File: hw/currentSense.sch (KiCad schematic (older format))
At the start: 2 parts, among them U601 ZXCT1086

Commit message: first pcb revision ready to order
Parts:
- renumbered U601 to U501
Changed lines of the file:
@@
 LIBS:usevolt
 LIBS:wurth_elektronik_LED
+LIBS:csb-cache
 EELAYER 26 0
 EELAYER END
@@
 $EndDescr
 $Comp
-L ZXCT1086 U601
+L ZXCT1086 U501
 U 1 1 594D8B7D
 P 5450 3600
-AR Path="/58BE52C9/58BE8E4D/594D8B7D" Ref="U601"  Part="1"
-AR Path="/58BE52C9/58BE8E7A/594D8B7D" Ref="U701"  Part="1"
-AR Path="/58BE52C9/5955DE03/594D8B7D" Ref="U801"  Part="1"
-AR Path="/58C7B0A8/594D8B80/594D8B7D" Ref="U1001"  Part="1"
-AR Path="/58C7B0A8/594D8B83/594D8B7D" Ref="U1101"  Part="1"
-AR Path="/58C7B0A8/58BE8E88/594D8B7D" Ref="U1201"  Part="1"
+AR Path="/59542AAB/595CED4D/594D8B7D" Ref="U501"  Part="1"
+AR Path="/59542AAB/58BE8E7A/594D8B7D" Ref="U601"  Part="1"
+AR Path="/59542AAB/58BE8E88/594D8B7D" Ref="U701"  Part="1"
+AR Path="/59542AAB/58BE8E96/594D8B7D" Ref="U801"  Part="1"
+AR Path="/5954FB0E/58BE8E4D/594D8B7D" Ref="U1001"  Part="1"
+AR Path="/5954FB0E/595CED50/594D8B7D" Ref="U1101"  Part="1"
+AR Path="/5954FB0E/595CED51/594D8B7D" Ref="U1201"  Part="1"
 F 0 "U1201" H 5425 3887 60  0000 C CNN
 F 1 "ZXCT1086" H 5425 3781 60  0000 C CNN
@@
 $EndComp
 $Comp
-L GND #PWR602
+L GND #PWR024
 U 1 1 594D8B7E
 P 5050 4000
-AR Path="/58BE52C9/58BE8E4D/594D8B7E" Ref="#PWR602"  Part="1"
-AR Path="/58BE52C9/58BE8E7A/594D8B7E" Ref="#PWR702"  Part="1"
-AR Path="/58BE52C9/5955DE03/594D8B7E" Ref="#PWR802"  Part="1"
-AR Path="/58C7B0A8/594D8B80/594D8B7E" Ref="#PWR1002"  Part="1"
-AR Path="/58C7B0A8/594D8B83/594D8B7E" Ref="#PWR1102"  Part="1"
-AR Path="/58C7B0A8/58BE8E88/594D8B7E" Ref="#PWR1202"  Part="1"
-F 0 "#PWR1202" H 5050 3750 50  0001 C CNN
+AR Path="/59542AAB/595CED4D/594D8B7E" Ref="#PWR024"  Part="1"
+AR Path="/59542AAB/58BE8E7A/594D8B7E" Ref="#PWR026"  Part="1"
+AR Path="/59542AAB/58BE8E88/594D8B7E" Ref="#PWR028"  Part="1"
+AR Path="/59542AAB/58BE8E96/594D8B7E" Ref="#PWR030"  Part="1"
+AR Path="/5954FB0E/58BE8E4D/594D8B7E" Ref="#PWR035"  Part="1"
+AR Path="/5954FB0E/595CED50/594D8B7E" Ref="#PWR037"  Part="1"
+AR Path="/5954FB0E/595CED51/594D8B7E" Ref="#PWR039"  Part="1"
+F 0 "#PWR039" H 5050 3750 50  0001 C CNN
 F 1 "GND" H 5055 3827 50  0000 C CNN
 F 2 "" H 5050 4000 50  0000 C CNN
@@
 $EndComp
 $Comp
-L +3V3 #PWR601
+L +3V3 #PWR025
 U 1 1 589841AE
 P 5050 3350
-AR Path="/58BE52C9/58BE8E4D/589841AE" Ref="#PWR601"  Part="1"
-AR Path="/58BE52C9/58BE8E7A/589841AE" Ref="#PWR701"  Part="1"
-AR Path="/58BE52C9/5955DE03/589841AE" Ref="#PWR801"  Part="1"
-AR Path="/58C7B0A8/594D8B80/589841AE" Ref="#PWR1001"  Part="1"
-AR Path="/58C7B0A8/594D8B83/589841AE" Ref="#PWR1101"  Part="1"
-AR Path="/58C7B0A8/58BE8E88/589841AE" Ref="#PWR1201"  Part="1"
-F 0 "#PWR1201" H 5050 3200 50  0001 C CNN
+AR Path="/59542AAB/595CED4D/589841AE" Ref="#PWR025"  Part="1"
+AR Path="/59542AAB/58BE8E7A/589841AE" Ref="#PWR027"  Part="1"
+AR Path="/59542AAB/58BE8E88/589841AE" Ref="#PWR029"  Part="1"
+AR Path="/59542AAB/58BE8E96/589841AE" Ref="#PWR031"  Part="1"
+AR Path="/5954FB0E/58BE8E4D/589841AE" Ref="#PWR036"  Part="1"
+AR Path="/5954FB0E/595CED50/589841AE" Ref="#PWR038"  Part="1"
+AR Path="/5954FB0E/595CED51/589841AE" Ref="#PWR040"  Part="1"
+F 0 "#PWR040" H 5050 3200 50  0001 C CNN
 F 1 "+3V3" H 5065 3523 50  0000 C CNN
 F 2 "" H 5050 3350 50  0000 C CNN
@@
 AR Path="/589A417E/589858BC" Ref="R?"  Part="1"
 AR Path="/58BE52C9/58BE8E88/589858BC" Ref="R?"  Part="1"
-AR Path="/58BE52C9/58BE8E4D/589858BC" Ref="R601"  Part="1"
-AR Path="/58BE52C9/58BE8E7A/589858BC" Ref="R701"  Part="1"
+AR Path="/58BE52C9/58BE8E4D/589858BC" Ref="R?"  Part="1"
+AR Path="/58BE52C9/58BE8E7A/589858BC" Ref="R?"  Part="1"
 AR Path="/58BE52C9/58BE8E96/589858BC" Ref="R?"  Part="1"
 AR Path="/58C7B0A8/58BE8E4D/589858BC" Ref="R?"  Part="1"
 AR Path="/58C7B0A8/58BE8E7A/589858BC" Ref="R?"  Part="1"
-AR Path="/58C7B0A8/58BE8E88/589858BC" Ref="R1201"  Part="1"
+AR Path="/58C7B0A8/58BE8E88/589858BC" Ref="R?"  Part="1"
 AR Path="/58C7B0A8/58BE8E96/589858BC" Ref="R?"  Part="1"
-AR Path="/58BE52C9/5955DE03/589858BC" Ref="R801"  Part="1"
-AR Path="/58C7B0A8/594D8B80/589858BC" Ref="R1001"  Part="1"
-AR Path="/58C7B0A8/594D8B83/589858BC" Ref="R1101"  Part="1"
+AR Path="/58BE52C9/5955DE03/589858BC" Ref="R?"  Part="1"
+AR Path="/58C7B0A8/594D8B80/589858BC" Ref="R?"  Part="1"
+AR Path="/58C7B0A8/594D8B83/589858BC" Ref="R?"  Part="1"
+AR Path="/59542AAB/58BE8E4D/589858BC" Ref="R?"  Part="1"
+AR Path="/59542AAB/58BE8E7A/589858BC" Ref="R601"  Part="1"
+AR Path="/59542AAB/58BE8E88/589858BC" Ref="R701"  Part="1"
+AR Path="/59542AAB/58BE8E96/589858BC" Ref="R801"  Part="1"
+AR Path="/5954FB0E/58BE8E4D/589858BC" Ref="R1001"  Part="1"
+AR Path="/5954FB0E/58BE8E7A/589858BC" Ref="R?"  Part="1"
+AR Path="/5954FB0E/58BE8E88/589858BC" Ref="R?"  Part="1"
+AR Path="/59542AAB/595CED4D/589858BC" Ref="R501"  Part="1"
+AR Path="/5954FB0E/595CED50/589858BC" Ref="R1101"  Part="1"
+AR Path="/5954FB0E/595CED51/589858BC" Ref="R1201"  Part="1"
 F 0 "R1201" V 6208 3508 45  0000 L CNN
 F 1 "LRMAT2512-R002FT4" V 6292 3508 45  0000 L CNN

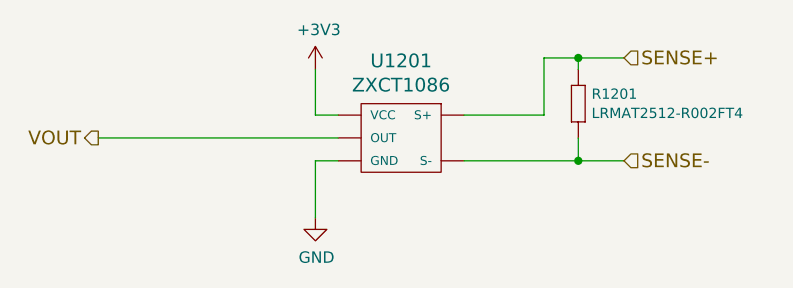
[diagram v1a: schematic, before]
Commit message: sw directory created, oil cooler added in hw
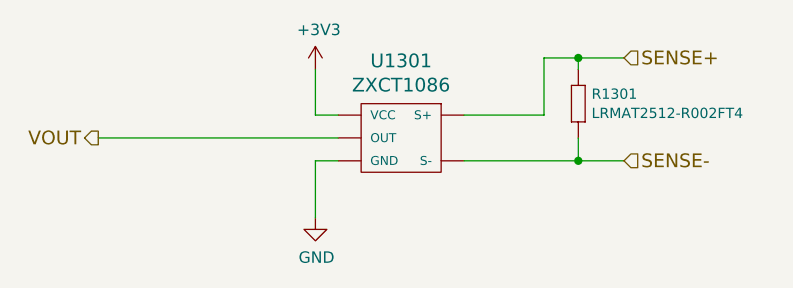
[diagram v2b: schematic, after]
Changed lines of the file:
@@
 $Descr A4 11693 8268
 encoding utf-8
-Sheet 11 12
+Sheet 11 13
 Title "MSB current sense sheet"
 Date "2017-02-05"
@@
 AR Path="/5954FB0E/595CED50/594D8B7D" Ref="U1101"  Part="1"
 AR Path="/5954FB0E/595CED51/594D8B7D" Ref="U1201"  Part="1"
-F 0 "U1201" H 5425 3887 60  0000 C CNN
+AR Path="/5954FB0E/59847685/594D8B7D" Ref="U1301"  Part="1"
+F 0 "U1301" H 5425 3887 60  0000 C CNN
 F 1 "ZXCT1086" H 5425 3781 60  0000 C CNN
 F 2 "usevolt:SOT-25" H 5100 4050 60  0001 C CNN
@@
 $EndComp
 $Comp
-L GND #PWR024
+L GND #PWR016
 U 1 1 594D8B7E
 P 5050 4000
-AR Path="/59542AAB/595CED4D/594D8B7E" Ref="#PWR024"  Part="1"
-AR Path="/59542AAB/58BE8E7A/594D8B7E" Ref="#PWR026"  Part="1"
-AR Path="/59542AAB/58BE8E88/594D8B7E" Ref="#PWR028"  Part="1"
-AR Path="/59542AAB/58BE8E96/594D8B7E" Ref="#PWR030"  Part="1"
-AR Path="/5954FB0E/58BE8E4D/594D8B7E" Ref="#PWR035"  Part="1"
-AR Path="/5954FB0E/595CED50/594D8B7E" Ref="#PWR037"  Part="1"
-AR Path="/5954FB0E/595CED51/594D8B7E" Ref="#PWR039"  Part="1"
-F 0 "#PWR039" H 5050 3750 50  0001 C CNN
+AR Path="/59542AAB/595CED4D/594D8B7E" Ref="#PWR016"  Part="1"
+AR Path="/59542AAB/58BE8E7A/594D8B7E" Ref="#PWR018"  Part="1"
+AR Path="/59542AAB/58BE8E88/594D8B7E" Ref="#PWR020"  Part="1"
+AR Path="/59542AAB/58BE8E96/594D8B7E" Ref="#PWR022"  Part="1"
+AR Path="/5954FB0E/58BE8E4D/594D8B7E" Ref="#PWR027"  Part="1"
+AR Path="/5954FB0E/595CED50/594D8B7E" Ref="#PWR029"  Part="1"
+AR Path="/5954FB0E/595CED51/594D8B7E" Ref="#PWR031"  Part="1"
+AR Path="/5954FB0E/59847685/594D8B7E" Ref="#PWR033"  Part="1"
+F 0 "#PWR033" H 5050 3750 50  0001 C CNN
 F 1 "GND" H 5055 3827 50  0000 C CNN
 F 2 "" H 5050 4000 50  0000 C CNN
@@
 $EndComp
 $Comp
-L +3V3 #PWR025
+L +3V3 #PWR017
 U 1 1 589841AE
 P 5050 3350
-AR Path="/59542AAB/595CED4D/589841AE" Ref="#PWR025"  Part="1"
-AR Path="/59542AAB/58BE8E7A/589841AE" Ref="#PWR027"  Part="1"
-AR Path="/59542AAB/58BE8E88/589841AE" Ref="#PWR029"  Part="1"
-AR Path="/59542AAB/58BE8E96/589841AE" Ref="#PWR031"  Part="1"
-AR Path="/5954FB0E/58BE8E4D/589841AE" Ref="#PWR036"  Part="1"
-AR Path="/5954FB0E/595CED50/589841AE" Ref="#PWR038"  Part="1"
-AR Path="/5954FB0E/595CED51/589841AE" Ref="#PWR040"  Part="1"
-F 0 "#PWR040" H 5050 3200 50  0001 C CNN
+AR Path="/59542AAB/595CED4D/589841AE" Ref="#PWR017"  Part="1"
+AR Path="/59542AAB/58BE8E7A/589841AE" Ref="#PWR019"  Part="1"
+AR Path="/59542AAB/58BE8E88/589841AE" Ref="#PWR021"  Part="1"
+AR Path="/59542AAB/58BE8E96/589841AE" Ref="#PWR023"  Part="1"
+AR Path="/5954FB0E/58BE8E4D/589841AE" Ref="#PWR028"  Part="1"
+AR Path="/5954FB0E/595CED50/589841AE" Ref="#PWR030"  Part="1"
+AR Path="/5954FB0E/595CED51/589841AE" Ref="#PWR032"  Part="1"
+AR Path="/5954FB0E/59847685/589841AE" Ref="#PWR034"  Part="1"
+F 0 "#PWR034" H 5050 3200 50  0001 C CNN
 F 1 "+3V3" H 5065 3523 50  0000 C CNN
 F 2 "" H 5050 3350 50  0000 C CNN
@@
 AR Path="/5954FB0E/595CED50/589858BC" Ref="R1101"  Part="1"
 AR Path="/5954FB0E/595CED51/589858BC" Ref="R1201"  Part="1"
-F 0 "R1201" V 6208 3508 45  0000 L CNN
+AR Path="/5954FB0E/59847685/589858BC" Ref="R1301"  Part="1"
+F 0 "R1301" V 6208 3508 45  0000 L CNN
 F 1 "LRMAT2512-R002FT4" V 6292 3508 45  0000 L CNN
 F 2 "usevolt:2512" H 6230 3600 20  0001 C CNN
